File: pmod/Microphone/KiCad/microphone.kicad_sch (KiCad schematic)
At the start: 16 parts, among them IC1 MAX4466EXK+T, J1 Conn_01x06_Pin

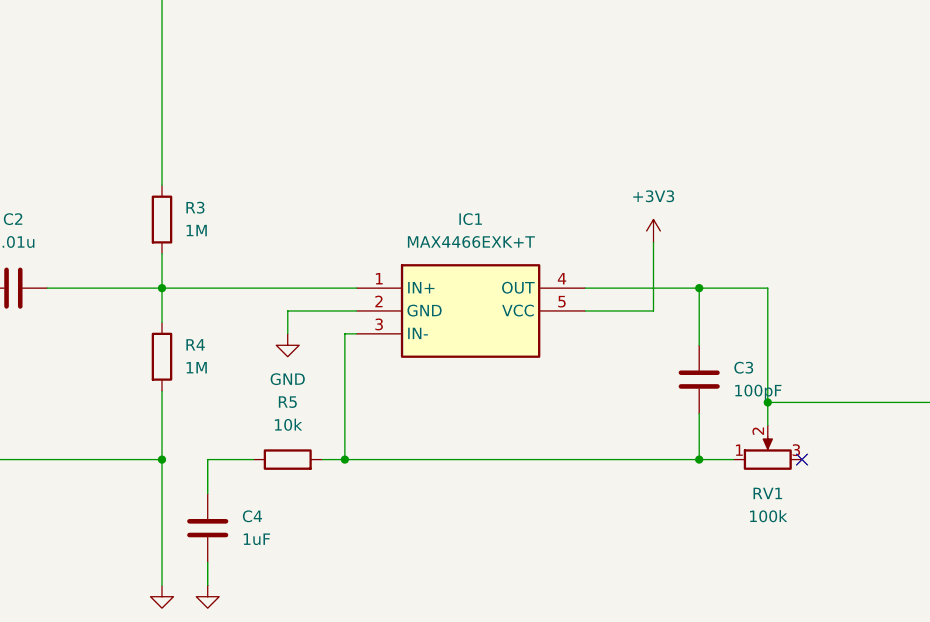
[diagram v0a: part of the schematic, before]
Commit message: Replace MAX4466 with LM321U
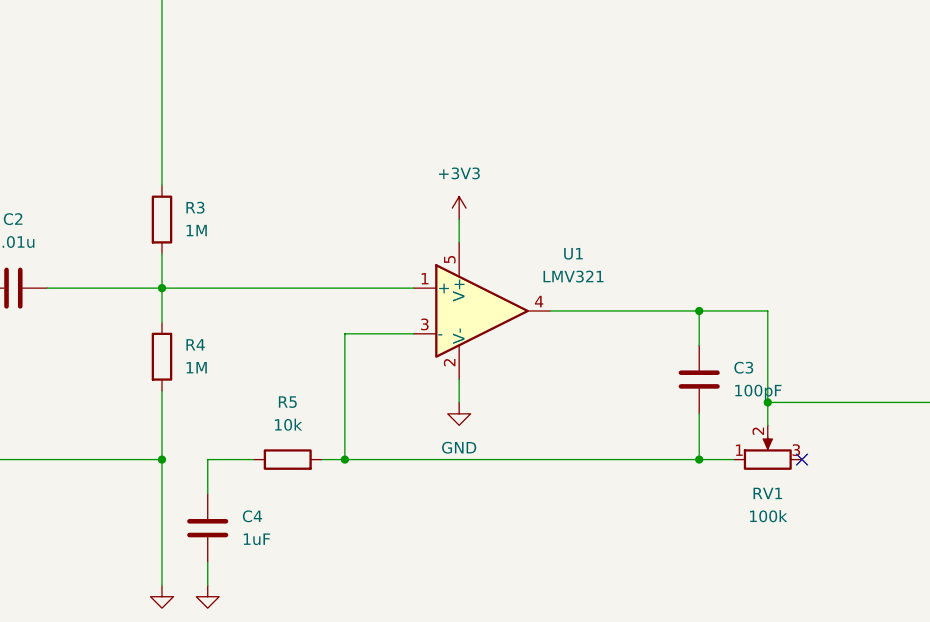
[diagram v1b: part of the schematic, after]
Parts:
- removed IC1: MAX4466EXK+T, SOT65P210X110-5N, symbol MAX4466EXK+T:MAX4466EXK+T
- added U1: LMV321, Package_TO_SOT_SMD:SOT-23-5, symbol Amplifier_Operational:LMV321
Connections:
- net +3V3: now also U1.5 (V+)
- net GND: now also U1.2 (V-)
- net at C3.2, R5.2, RV1.1: now also U1.3 (-)
- net at C3.1, J1.1 (Pin_1), RV1.2: now also U1.4
- net at C2.2, R3.2, R4.1: now also U1.1 (+)

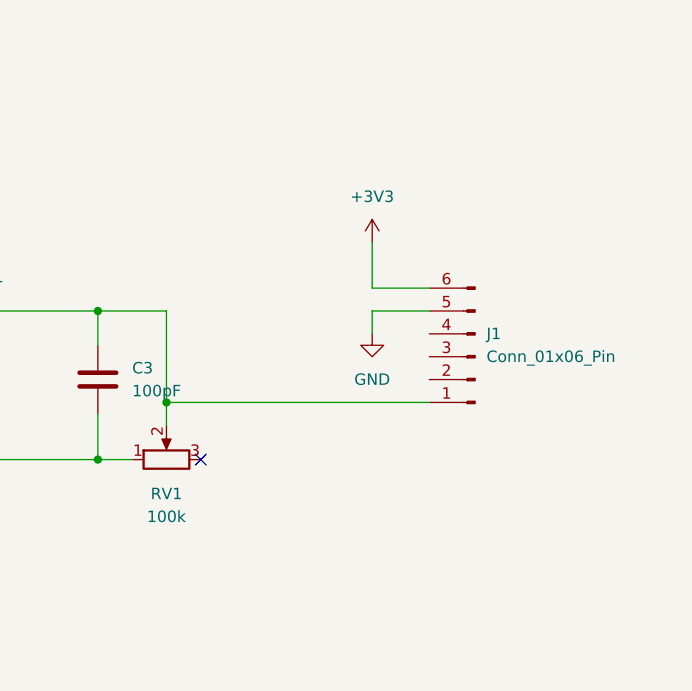
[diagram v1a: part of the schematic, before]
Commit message: Flip P-MOD connector to align with OG PMOD devices and add Mouser hyperlink for the opamp
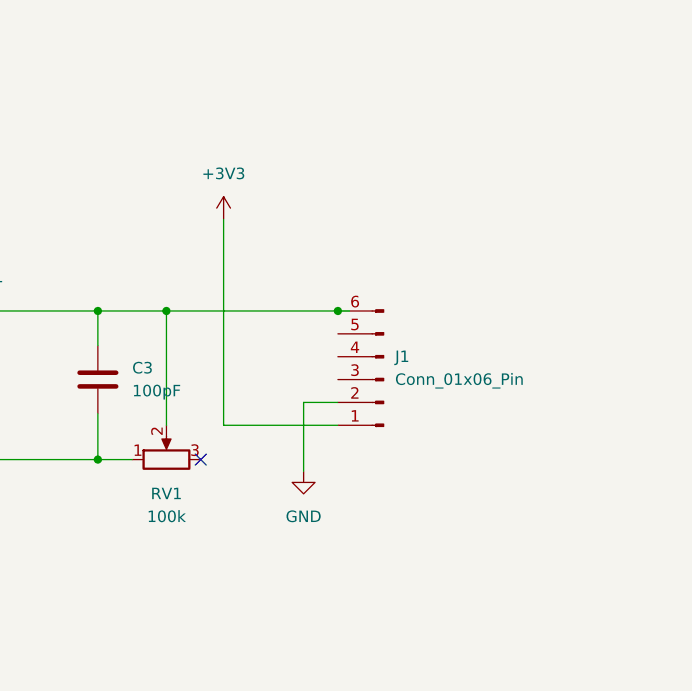
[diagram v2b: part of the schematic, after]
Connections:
- net +3V3: now also J1.1 (Pin_1); no longer J1.6 (Pin_6)
- net GND: now also J1.2 (Pin_2); no longer J1.5 (Pin_5)
- net at C3.1, RV1.2, U1.4: now also J1.6 (Pin_6); no longer J1.1 (Pin_1)
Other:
- moved on the sheet: J1
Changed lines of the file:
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@@
+	)
+	(junction
+		(at 217.17 77.47)
+		(diameter 0)
+		(color 0 0 0 0)
+	)
+	(junction
+		(at 236.22 77.47)
+		(diameter 0)
+		(color 0 0 0 0)
 	)
 	(junction
@@
 	)
 	(junction
-		(at 217.17 87.63)
-		(diameter 0)
-		(color 0 0 0 0)
-	)
-	(junction
 		(at 149.86 93.98)
 		(diameter 0)
@@
 	(wire
 		(pts
+			(xy 217.17 77.47) (xy 236.22 77.47)
+		)
+		(stroke
+			(width 0)
+			(type default)
+		)
+	)
+	(wire
+		(pts
 			(xy 170.18 93.98) (xy 167.64 93.98)
 		)
@@
 	(wire
 		(pts
+			(xy 232.41 87.63) (xy 232.41 95.25)
+		)
+		(stroke
+			(width 0)
+			(type default)
+		)
+	)
+	(wire
+		(pts
 			(xy 149.86 74.93) (xy 177.8 74.93)
 		)
@@
 	(wire
 		(pts
-			(xy 217.17 77.47) (xy 217.17 87.63)
-		)
-		(stroke
-			(width 0)
-			(type default)
-		)
-	)
-	(wire
-		(pts
 			(xy 170.18 80.01) (xy 177.8 80.01)
 		)
@@
 	(wire
 		(pts
-			(xy 240.03 74.93) (xy 246.38 74.93)
-		)
-		(stroke
-			(width 0)
-			(type default)
-		)
-	)
-	(wire
-		(pts
 			(xy 92.71 74.93) (xy 92.71 78.74)
 		)
@@
 	(wire
 		(pts
+			(xy 236.22 87.63) (xy 232.41 87.63)
+		)
+		(stroke
+			(width 0)
+			(type default)
+		)
+	)
+	(wire
+		(pts
 			(xy 137.16 74.93) (xy 149.86 74.93)
 		)
@@
 	(wire
 		(pts
-			(xy 217.17 87.63) (xy 217.17 90.17)
+			(xy 217.17 77.47) (xy 217.17 90.17)
 		)
 		(stroke
@@
 	(wire
 		(pts
-			(xy 240.03 77.47) (xy 246.38 77.47)
-		)
-		(stroke
-			(width 0)
-			(type default)
-		)
-	)
-	(wire
-		(pts
 			(xy 100.33 62.23) (xy 100.33 74.93)
 		)
@@
 	(wire
 		(pts
-			(xy 240.03 69.85) (xy 240.03 74.93)
-		)
-		(stroke
-			(width 0)
-			(type default)
-		)
-	)
-	(wire
-		(pts
 			(xy 154.94 105.41) (xy 154.94 107.95)
 		)
@@
 	(wire
 		(pts
+			(xy 237.49 77.47) (xy 236.22 77.47)
+		)
+		(stroke
+			(width 0)
+			(type default)
+		)
+	)
+	(wire
+		(pts
 			(xy 209.55 77.47) (xy 209.55 81.28)
 		)
@@
 	(wire
 		(pts
-			(xy 240.03 80.01) (xy 240.03 77.47)
+			(xy 223.52 67.31) (xy 223.52 90.17)
 		)
 		(stroke
@@
 	(wire
 		(pts
-			(xy 217.17 87.63) (xy 246.38 87.63)
-		)
-		(stroke
-			(width 0)
-			(type default)
-		)
-	)
-	(wire
-		(pts
 			(xy 100.33 49.53) (xy 100.33 52.07)
+		)
+		(stroke
+			(width 0)
+			(type default)
+		)
+	)
+	(wire
+		(pts
+			(xy 236.22 90.17) (xy 223.52 90.17)
 		)
 		(stroke
@@
 	(symbol
 		(lib_id "Connector:Conn_01x06_Pin")
-		(at 251.46 82.55 180)
+		(at 241.3 85.09 180)
 		(unit 1)
 		(exclude_from_sim no)
@@
 		(fields_autoplaced yes)
 		(property "Reference" "J1"
-			(at 252.73 80.0099 0)
+			(at 242.57 82.5499 0)
 			(effects
 				(font
@@
 		)
 		(property "Value" "Conn_01x06_Pin"
-			(at 252.73 82.5499 0)
+			(at 242.57 85.0899 0)
 			(effects
 				(font
@@
 		)
 		(property "Footprint" "Connector_PinHeader_2.54mm:PinHeader_1x06_P2.54mm_Horizontal"
-			(at 251.46 82.55 0)
+			(at 241.3 85.09 0)
 			(effects
 				(font
@@
 		)
 		(property "Datasheet" "~"
-			(at 251.46 82.55 0)
+			(at 241.3 85.09 0)
 			(effects
 				(font
@@
 		)
 		(property "Description" "Generic connector, single row, 01x06, script generated"
-			(at 251.46 82.55 0)
+			(at 241.3 85.09 0)
 			(effects
 				(font
@@
 	)
 	(symbol
-		(lib_id "power:+3V3")
-		(at 240.03 69.85 0)
-		(unit 1)
-		(exclude_from_sim no)
-		(in_bom yes)
-		(on_board yes)
-		(dnp no)
-		(fields_autoplaced yes)
-		(property "Reference" "#PWR9"
-			(at 240.03 73.66 0)
-			(effects
-				(font
-					(size 1.27 1.27)
-				)
-				(hide yes)
-			)
-		)
-		(property "Value" "+3V3"
-			(at 240.03 64.77 0)
-			(effects
-				(font
-					(size 1.27 1.27)
-				)
-			)
-		)
-		(property "Footprint" ""
-			(at 240.03 69.85 0)
-			(effects
-				(font
-					(size 1.27 1.27)
-				)
-				(hide yes)
-			)
-		)
-		(property "Datasheet" ""
-			(at 240.03 69.85 0)
-			(effects
-				(font
-					(size 1.27 1.27)
-				)
-				(hide yes)
-			)
-		)
-		(property "Description" "Power symbol creates a global label with name \"+3V3\""
-			(at 240.03 69.85 0)
-			(effects
-				(font
-					(size 1.27 1.27)
-				)
-				(hide yes)
-			)
-		)
-		(pin "1"
-		)
-		(instances
-			(project ""
-				(path "/2a9bcfd4-adab-4e02-ac26-fb85a4426adb"
-					(reference "#PWR9")
-					(unit 1)
-				)
-			)
-		)
-	)
-	(symbol
 		(lib_id "Mechanical:MountingHole")
 		(at 255.27 25.4 0)
@@
 				(path "/2a9bcfd4-adab-4e02-ac26-fb85a4426adb"
 					(reference "H2")
+					(unit 1)
+				)
+			)
+		)
+	)
+	(symbol
+		(lib_id "power:GND")
+		(at 232.41 95.25 0)
+		(unit 1)
+		(exclude_from_sim no)
+		(in_bom yes)
+		(on_board yes)
+		(dnp no)
+		(fields_autoplaced yes)
+		(property "Reference" "#PWR8"
+			(at 232.41 101.6 0)
+			(effects
+				(font
+					(size 1.27 1.27)
+				)
+				(hide yes)
+			)
+		)
+		(property "Value" "GND"
+			(at 232.41 100.33 0)
+			(effects
+				(font
+					(size 1.27 1.27)
+				)
+			)
+		)
+		(property "Footprint" ""
+			(at 232.41 95.25 0)
+			(effects
+				(font
+					(size 1.27 1.27)
+				)
+				(hide yes)
+			)
+		)
+		(property "Datasheet" ""
+			(at 232.41 95.25 0)
+			(effects
+				(font
+					(size 1.27 1.27)
+				)
+				(hide yes)
+			)
+		)
+		(property "Description" "Power symbol creates a global label with name \"GND\" , ground"
+			(at 232.41 95.25 0)
+			(effects
+				(font
+					(size 1.27 1.27)
+				)
+				(hide yes)
+			)
+		)
+		(pin "1"
+		)
+		(instances
+			(project ""
+				(path "/2a9bcfd4-adab-4e02-ac26-fb85a4426adb"
+					(reference "#PWR8")
 					(unit 1)
 				)
@@
 	)
 	(symbol
-		(lib_id "power:GND")
-		(at 240.03 80.01 0)
+		(lib_id "power:+3V3")
+		(at 223.52 67.31 0)
 		(unit 1)
 		(exclude_from_sim no)
@@
 		(dnp no)
 		(fields_autoplaced yes)
-		(property "Reference" "#PWR8"
-			(at 240.03 86.36 0)
-			(effects
-				(font
-					(size 1.27 1.27)
-				)
-				(hide yes)
-			)
-		)
-		(property "Value" "GND"
-			(at 240.03 85.09 0)
+		(property "Reference" "#PWR9"
+			(at 223.52 71.12 0)
+			(effects
+				(font
+					(size 1.27 1.27)
+				)
+				(hide yes)
+			)
+		)
+		(property "Value" "+3V3"
+			(at 223.52 62.23 0)
 			(effects
 				(font
@@
 		)
 		(property "Footprint" ""
-			(at 240.03 80.01 0)
+			(at 223.52 67.31 0)
 			(effects
 				(font
@@
 		)
 		(property "Datasheet" ""
-			(at 240.03 80.01 0)
-			(effects
-				(font
-					(size 1.27 1.27)
-				)
-				(hide yes)
-			)
-		)
-		(property "Description" "Power symbol creates a global label with name \"GND\" , ground"
-			(at 240.03 80.01 0)
+			(at 223.52 67.31 0)
+			(effects
+				(font
+					(size 1.27 1.27)
+				)
+				(hide yes)
+			)
+		)
+		(property "Description" "Power symbol creates a global label with name \"+3V3\""
+			(at 223.52 67.31 0)
 			(effects
 				(font
@@
 			(project ""
 				(path "/2a9bcfd4-adab-4e02-ac26-fb85a4426adb"
-					(reference "#PWR8")
+					(reference "#PWR9")
 					(unit 1)
 				)

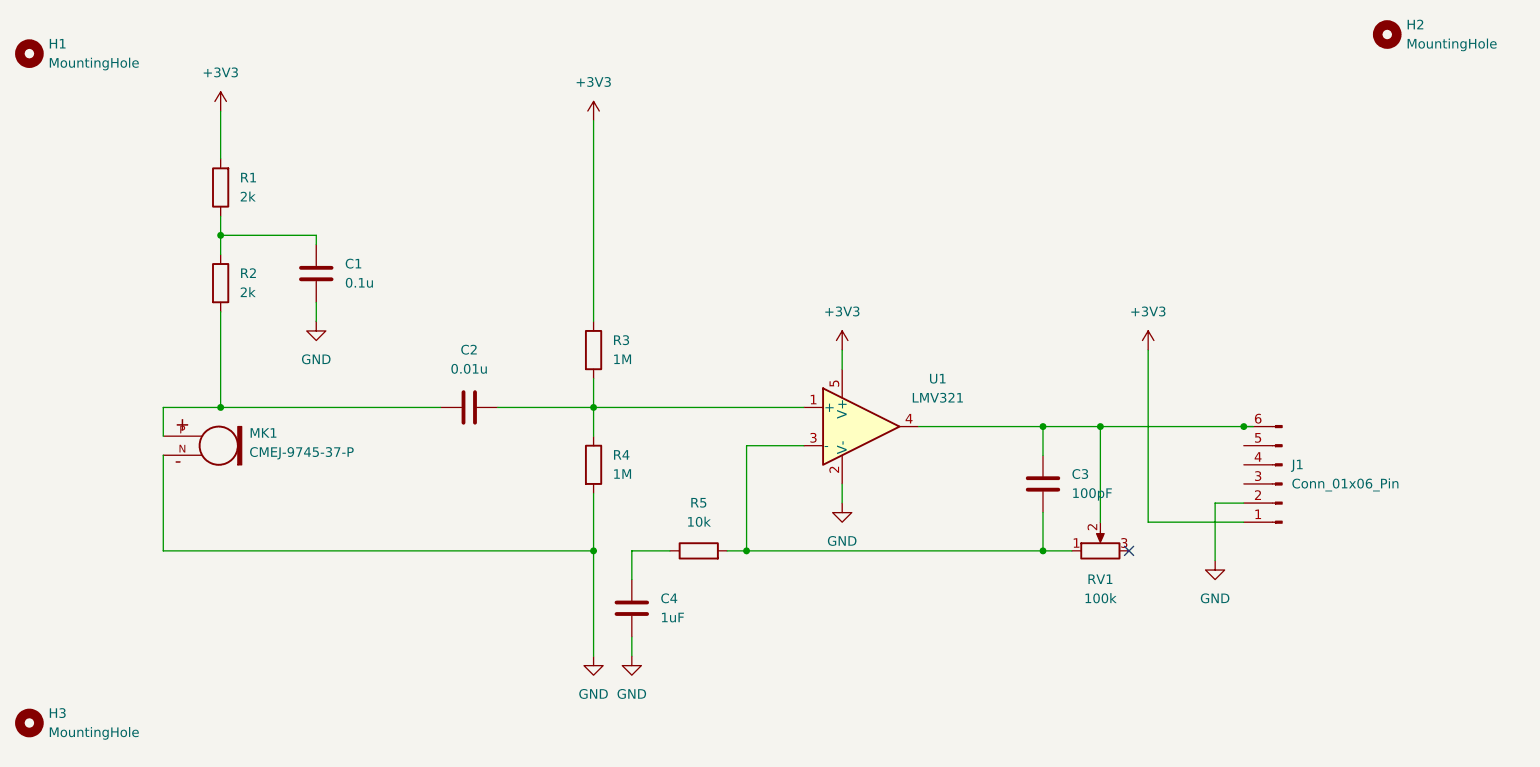
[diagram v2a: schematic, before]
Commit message: Add fourth hole
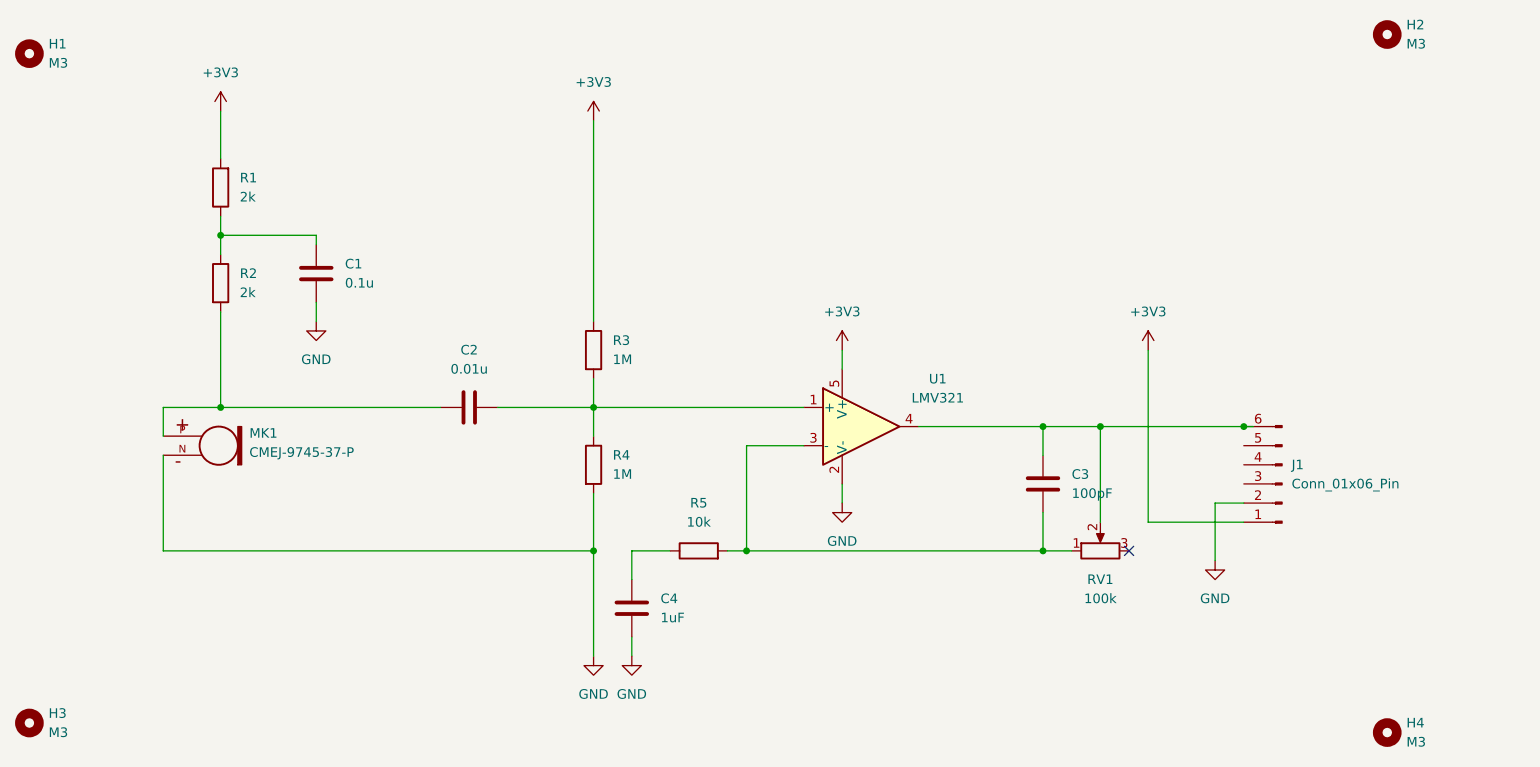
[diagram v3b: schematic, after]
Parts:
- added H4: M3, MountingHole:MountingHole_3.2mm_M3, symbol Mechanical:MountingHole
- H1, H2, H3: value MountingHole -> M3
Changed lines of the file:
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@@
+	)
+	(symbol
+		(lib_id "Mechanical:MountingHole")
+		(at 255.27 118.11 0)
+		(unit 1)
+		(exclude_from_sim yes)
+		(in_bom no)
+		(on_board yes)
+		(dnp no)
+		(fields_autoplaced yes)
+		(property "Reference" "H4"
+			(at 257.81 116.8399 0)
+			(effects
+				(font
+					(size 1.27 1.27)
+				)
+				(justify left)
+			)
+		)
+		(property "Value" "M3"
+			(at 257.81 119.3799 0)
+			(effects
+				(font
+					(size 1.27 1.27)
+				)
+				(justify left)
+			)
+		)
+		(property "Footprint" "MountingHole:MountingHole_3.2mm_M3"
+			(at 255.27 118.11 0)
+			(effects
+				(font
+					(size 1.27 1.27)
+				)
+				(hide yes)
+			)
+		)
+		(property "Datasheet" "~"
+			(at 255.27 118.11 0)
+			(effects
+				(font
+					(size 1.27 1.27)
+				)
+				(hide yes)
+			)
+		)
+		(property "Description" "Mounting Hole without connection"
+			(at 255.27 118.11 0)
+			(effects
+				(font
+					(size 1.27 1.27)
+				)
+				(hide yes)
+			)
+		)
+		(instances
+			(project "microphone"
+				(path "/2a9bcfd4-adab-4e02-ac26-fb85a4426adb"
+					(reference "H4")
+					(unit 1)
+				)
+			)
+		)
 	)
 	(symbol
@@
 			)
 		)
-		(property "Value" "MountingHole"
+		(property "Value" "M3"
 			(at 257.81 26.6699 0)
 			(effects
@@
 			)
 		)
-		(property "Value" "MountingHole"
+		(property "Value" "M3"
 			(at 77.47 118.1099 0)
 			(effects
@@
 			)
 		)
-		(property "Value" "MountingHole"
+		(property "Value" "M3"
 			(at 77.47 29.2099 0)
 			(effects

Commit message: Changed R1 R2 an C1 to suit the datasheet of the electret
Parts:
- C1: value 0.1u -> 0.2u
- R1, R2: value 2k -> 1k
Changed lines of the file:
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@@
 			)
 		)
-		(property "Value" "0.1u"
+		(property "Value" "0.2u"
 			(at 116.84 58.4199 0)
 			(effects
@@
 			)
 		)
-		(property "Value" "2k"
+		(property "Value" "1k"
 			(at 102.87 59.6899 0)
 			(effects
@@
 			)
 		)
-		(property "Value" "2k"
+		(property "Value" "1k"
 			(at 102.87 46.9899 0)
 			(effects
